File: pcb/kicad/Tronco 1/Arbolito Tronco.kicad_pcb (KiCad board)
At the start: 2 copper layers, 68.2 x 100.6 mm, 35 parts, among them U1 WS2812B, U10 WS2812B, U11 WS2812B, U12 WS2812B, U2 WS2812B, U3 WS2812B, U4 WS2812B, U5 WS2812B, U6 WS2812B, U7 WS2812B, U8 WS2812B, U9 WS2812B

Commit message: Do some cleaning and add .gitignore
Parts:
- removed U10, U9: WS2812B, LED_SMD:LED_WS2812B_PLCC4_5.0x5.0mm_P3.2mm
- removed the U3 at (125.8, 80.6)
- removed the U4 at (125.8, 80.6)
- added J1: Conn_01x01, Library:Input, F.Cu at (138.0, 128.8)
- added J10: Conn_01x01, Library:Output, F.Cu at (141.1, 62.1)
- added J11: Conn_01x01, Library:Output, F.Cu at (137.8, 68.1)
- added J12: Conn_01x01, Library:Output, F.Cu at (141.2, 68.1)
- added J2: Conn_01x01, Library:Input, F.Cu at (141.1, 128.8)
- added J3: Conn_01x01, Library:Input, F.Cu at (132.0, 128.8)
- added J4: Conn_01x01, Library:Input, F.Cu at (135.0, 128.8)
- added J5: Conn_01x01, Library:Input, F.Cu at (144.0, 128.8)
- added J6: Conn_01x01, Library:Input, F.Cu at (147.0, 128.8)
- added J7: Conn_01x01, Library:Output, F.Cu at (141.2, 65.1)
- added J8: Conn_01x01, Library:Output, F.Cu at (137.8, 65.1)
- added J9: Conn_01x01, Library:Output, F.Cu at (137.9, 62.1)
- U1, U2: footprint LED_SMD:LED_WS2812B_PLCC4_5.0x5.0mm_P3.2mm -> Library:LED_WS2812B_PLCC4_5.0x5.0mm_P3.2mm
- U3: renamed from U5; footprint LED_SMD:LED_WS2812B_PLCC4_5.0x5.0mm_P3.2mm -> Library:LED_WS2812B_PLCC4_5.0x5.0mm_P3.2mm
- U4: renamed from U6; footprint LED_SMD:LED_WS2812B_PLCC4_5.0x5.0mm_P3.2mm -> Library:LED_WS2812B_PLCC4_5.0x5.0mm_P3.2mm
- U5: renamed from U7; footprint LED_SMD:LED_WS2812B_PLCC4_5.0x5.0mm_P3.2mm -> Library:LED_WS2812B_PLCC4_5.0x5.0mm_P3.2mm
- U6: renamed from U8; footprint LED_SMD:LED_WS2812B_PLCC4_5.0x5.0mm_P3.2mm -> Library:LED_WS2812B_PLCC4_5.0x5.0mm_P3.2mm
- U7: renamed from U11; footprint LED_SMD:LED_WS2812B_PLCC4_5.0x5.0mm_P3.2mm -> Library:LED_WS2812B_PLCC4_5.0x5.0mm_P3.2mm
- U8: renamed from U12; footprint LED_SMD:LED_WS2812B_PLCC4_5.0x5.0mm_P3.2mm -> Library:LED_WS2812B_PLCC4_5.0x5.0mm_P3.2mm
- moved C6 30.3 mm to (146.4, 54.2)
- moved C1 26.3 mm to (146.3, 54.2)
- renumbered C11 to C1, C12 to C2, C13 to C3, C14 to C4, C15 to C5, C16 to C6
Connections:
- U3 pad 4: Net-(U4-DOUT) (its old number) -> Net-(U2-DOUT)
- U6 pad 2: Net-(U8-DOUT) -> Net-(U6-DOUT)
- U7 pad 4: Net-(U10-DOUT) -> Net-(U6-DOUT)
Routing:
- net Net-(U6-DOUT): track 0.00 -> 65.4 mm, vias 0 -> 1
- net Net-(U4-DOUT) (its old number): track 42.1 -> 0.00 mm
- net Net-(U10-DOUT): track 39.1 -> 0.00 mm
- net Net-(U8-DOUT): track 32.0 -> 0.00 mm
- net Net-(U2-DOUT): track 49.5 -> 74.9 mm, vias 0 -> 1
- net GND: track 40.2 -> 54.8 mm, vias 9 -> 11
- net Net-(U10-DIN): track 3.41 -> 0.00 mm, vias 1 -> 0
- net Net-(U3-DOUT) (its old number): track 3.40 -> 0.00 mm, vias 1 -> 0
- net Net-(U4-DOUT): track 64.5 -> 66.0 mm
- net +5V: track 15.8 -> 15.4 mm, vias 9 -> 11
- removed copper zone on B.Cu, net +5V
- removed copper zone on B.Cu, net /DIN
- removed copper zone on F.Cu, net /DIN
- removed copper zone on B.Cu, net /Dout
- removed copper zone on F.Cu, net /Dout
- removed copper zone on F.Cu, net GND
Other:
- board size 68.2 x 100.6 mm -> 68.2 x 102.6 mm

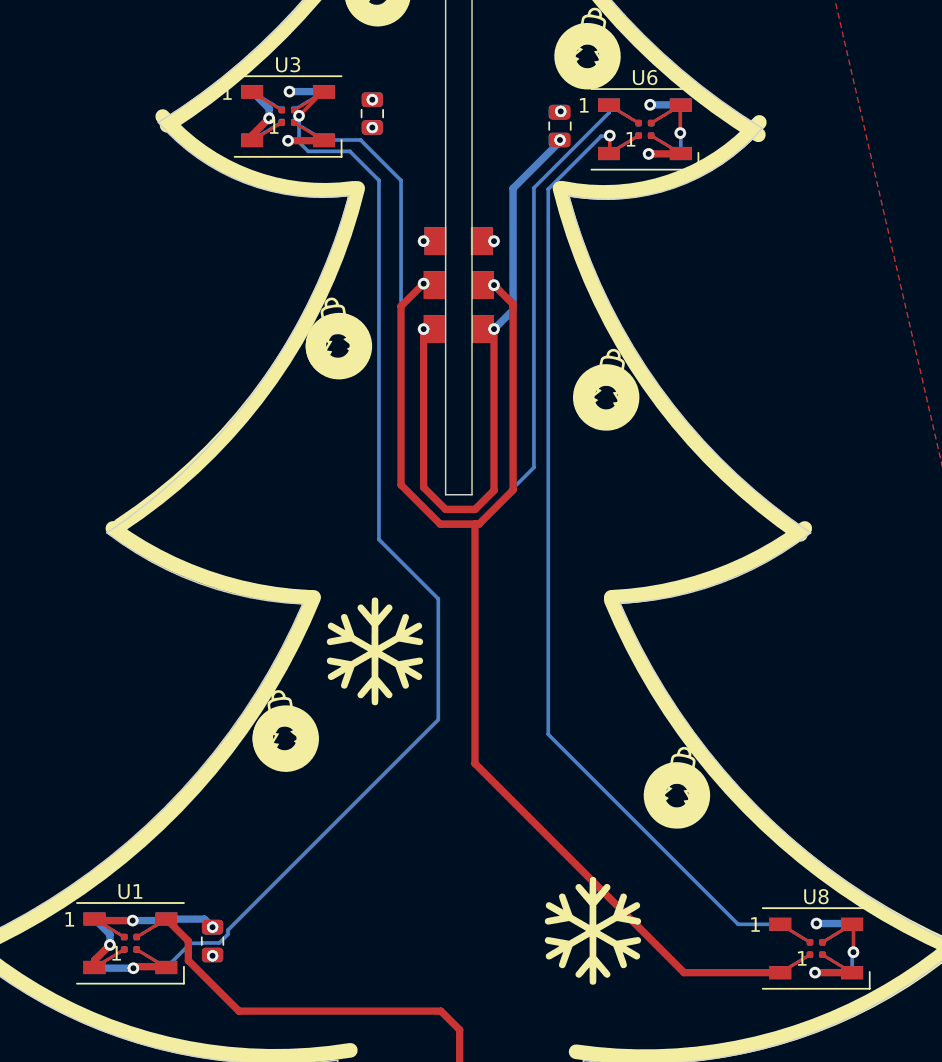
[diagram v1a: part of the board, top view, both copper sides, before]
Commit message: Led Shorts fixed
Vias were shorting leds pins, should be fixed :)
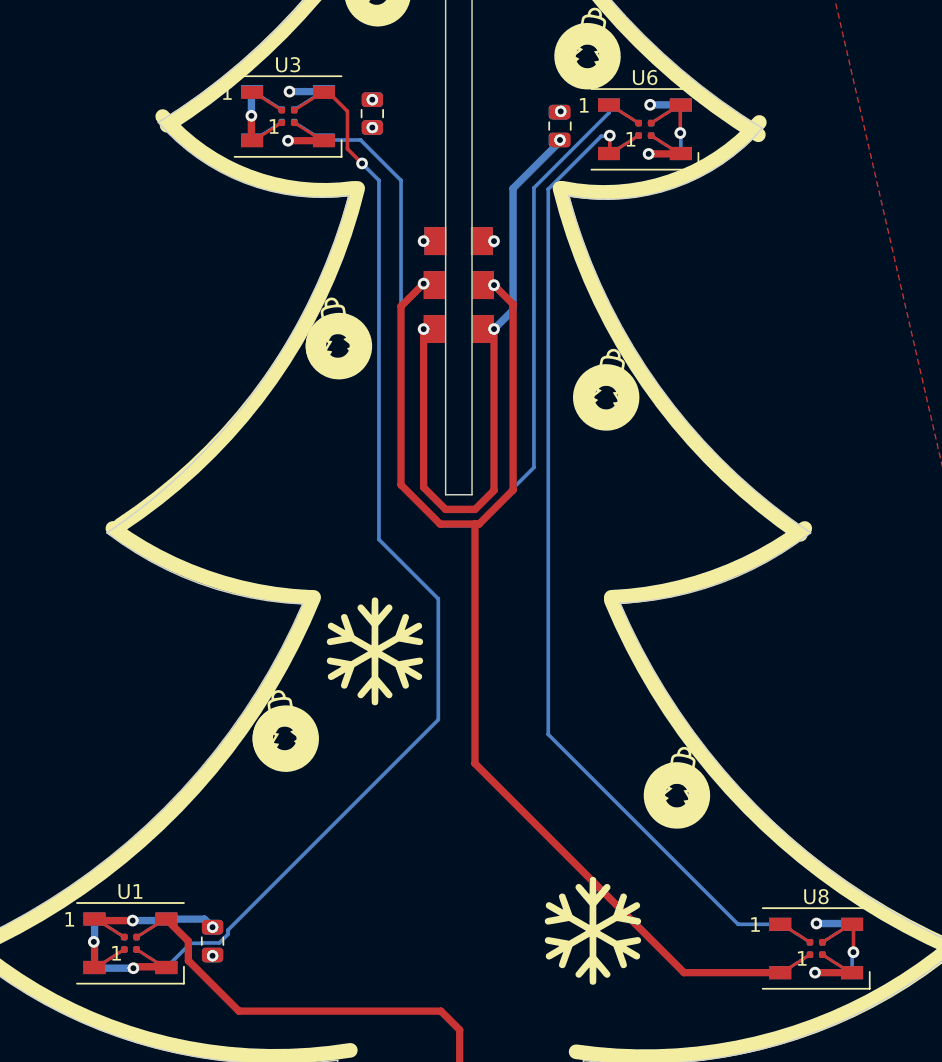
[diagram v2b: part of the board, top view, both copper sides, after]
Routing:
- net Net-(U2-DOUT): track 74.9 -> 71.5 mm
- net Net-(U1-DOUT): track 4.17 -> 3.34 mm
- net Net-(U3-DOUT): track 4.55 -> 3.76 mm

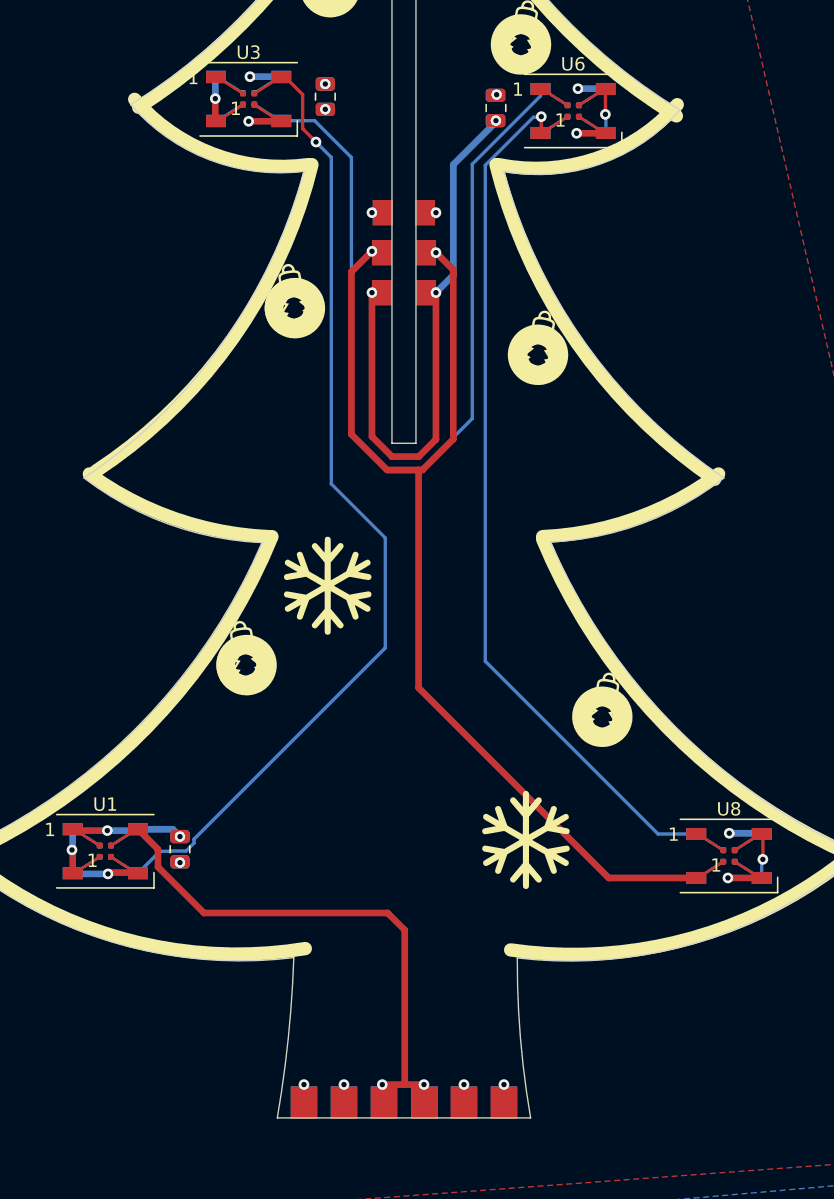
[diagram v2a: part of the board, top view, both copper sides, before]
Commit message: DRC Errors fixeds
The WS218B double footprint was remade in order to avoid DRC errors :3
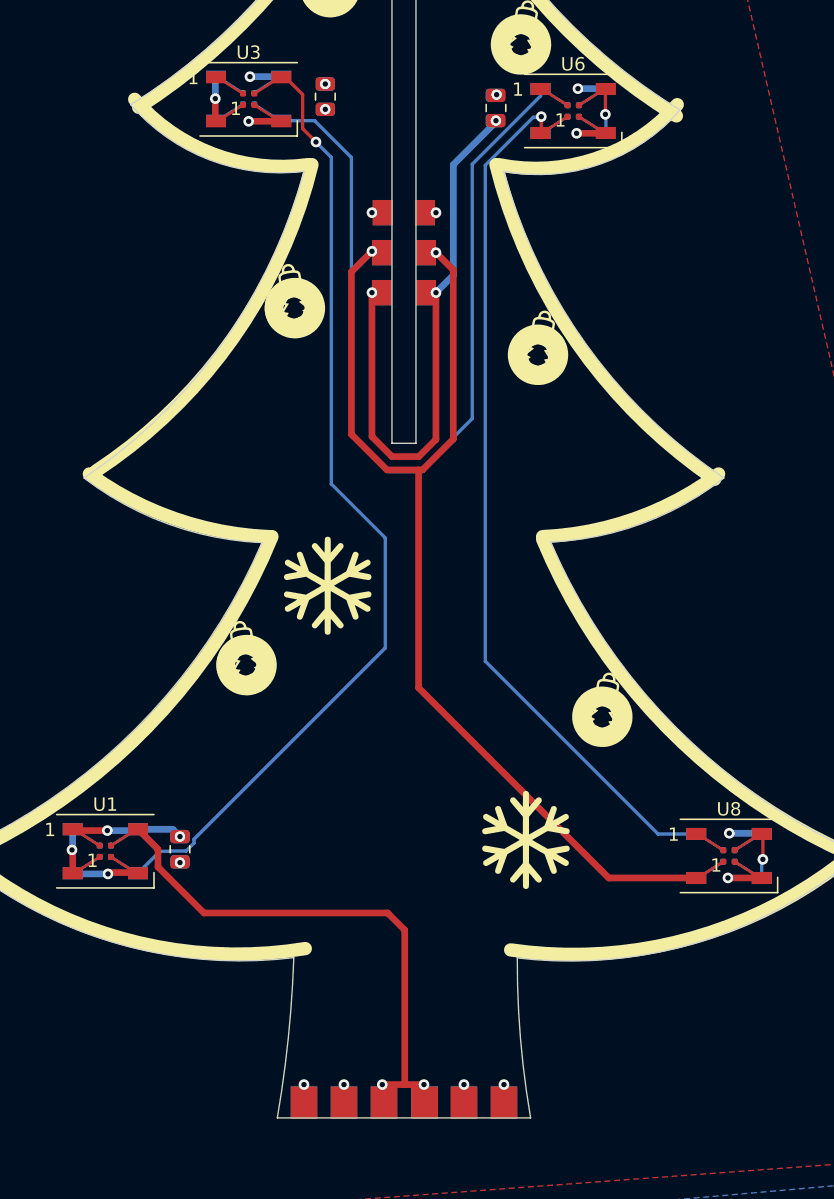
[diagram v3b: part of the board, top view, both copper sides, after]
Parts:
- added J13: Conn_01x01, Library:Input, B.Cu at (141.1, 128.8)
- added J14: Conn_01x01, Library:Input, B.Cu at (138.0, 128.8)
- added J15: Conn_01x01, Library:Input, B.Cu at (132.0, 128.8)
- added J16: Conn_01x01, Library:Input, B.Cu at (135.0, 128.8)
- added J17: Conn_01x01, Library:Input, B.Cu at (144.0, 128.8)
- added J18: Conn_01x01, Library:Input, B.Cu at (147.0, 128.8)
- added J19: Conn_01x01, Library:Output, B.Cu at (141.2, 65.1)
- added J20: Conn_01x01, Library:Output, B.Cu at (137.8, 65.1)
- added J21: Conn_01x01, Library:Output, B.Cu at (137.9, 62.1)
- added J22: Conn_01x01, Library:Output, B.Cu at (141.1, 62.1)
- added J23: Conn_01x01, Library:Output, B.Cu at (141.2, 68.1)
- added J24: Conn_01x01, Library:Output, B.Cu at (137.8, 68.1)
